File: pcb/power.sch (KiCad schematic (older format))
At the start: 8 parts

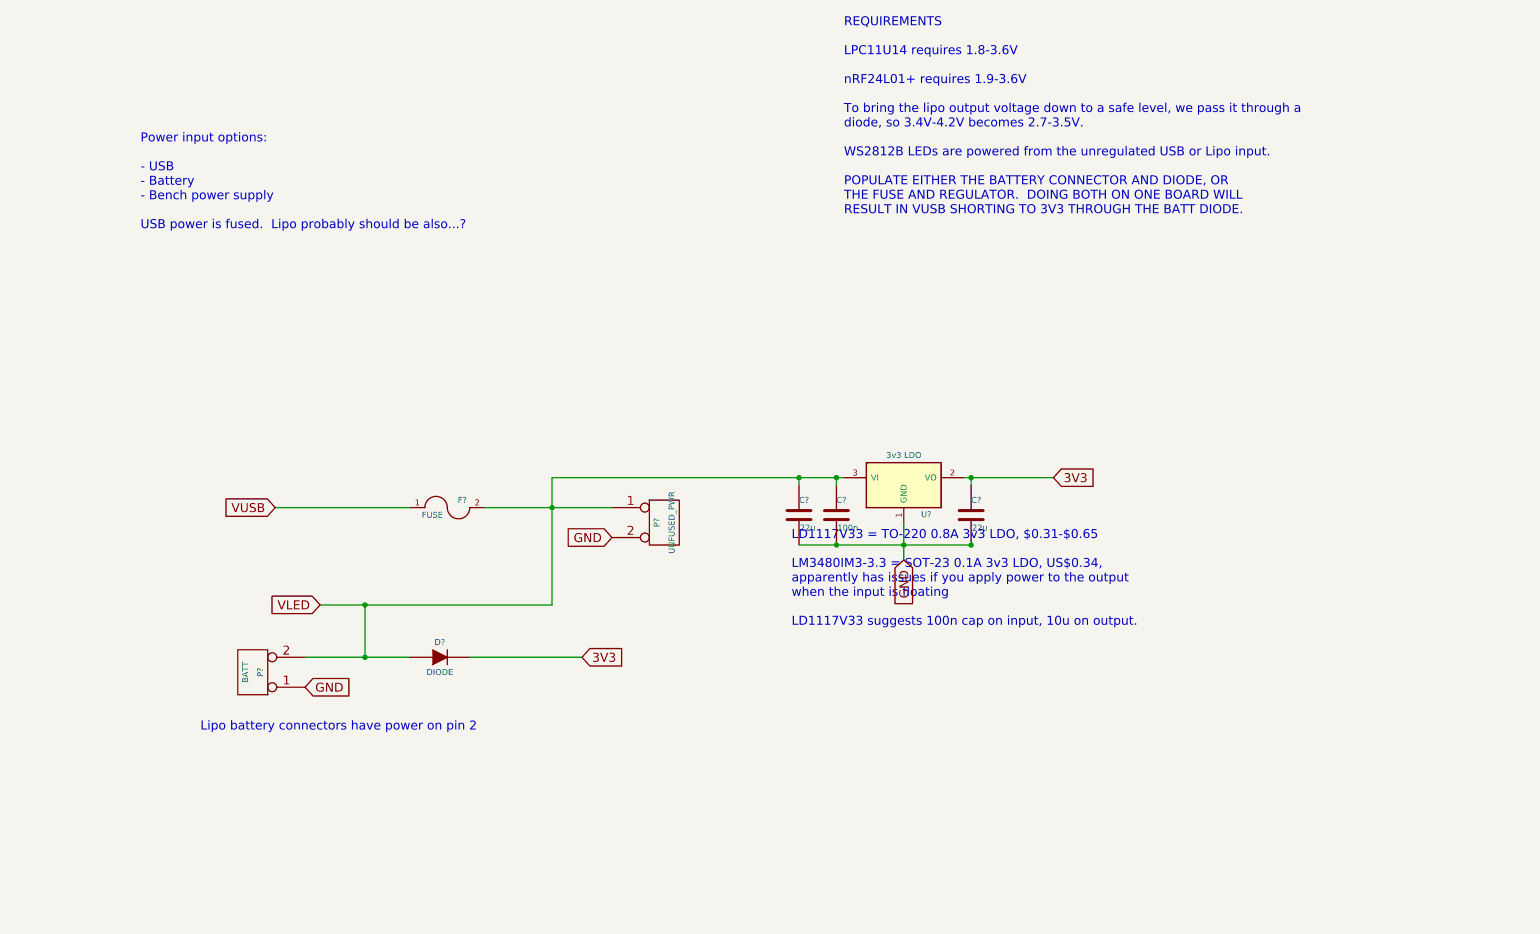
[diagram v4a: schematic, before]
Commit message: added second 3v3 ldo in parallel with the first one, so we can have the option at build time
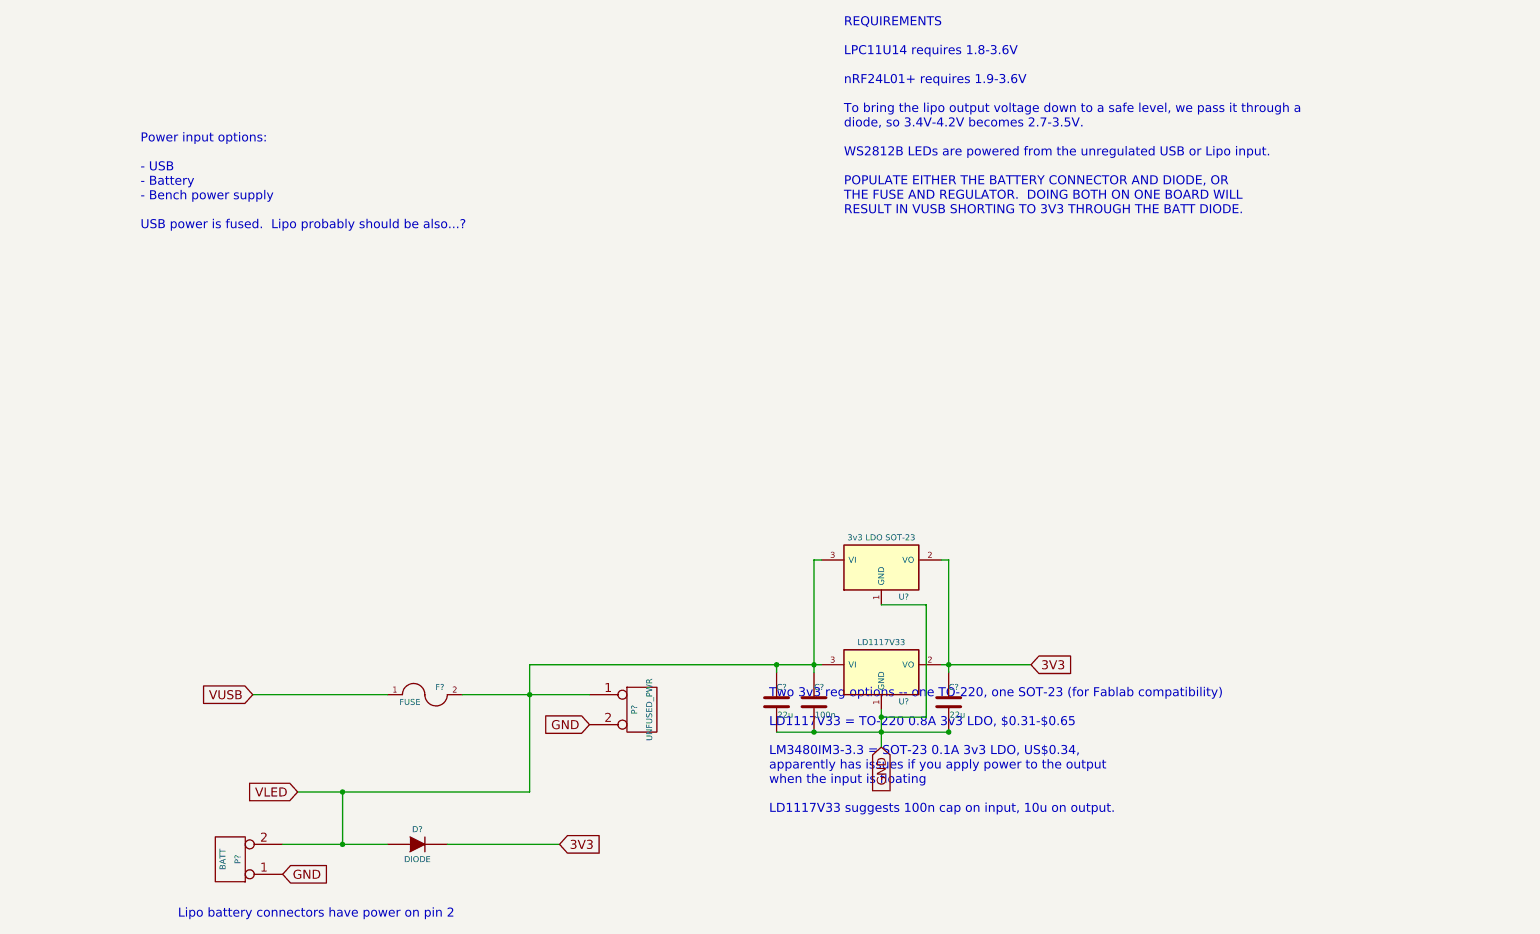
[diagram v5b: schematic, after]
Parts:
- added U?: 3v3 LDO SOT-23, ~, symbol NCP1117ST33T3G
- U?: value 3v3 LDO -> LD1117V33
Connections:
- net 3V3: now also U?.2 (VO)
- net GND: now also U?.1 (GND)
- net VLED: now also U?.3 (VI)
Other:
- note added: "Two 3v3 reg options -- one TO-220, one SOT-23 (for Fablab compatibility)\n\nLD1117V33 = TO-220 0.8A 3v3 LDO, $0.31-$0.65\n\nLM3480IM3-3.3 = SOT-23 0.1A 3v3 LDO, US$0.34,\napparently has issues if you apply power to the output\nwhen the input is floating\n\nLD1117V33 suggests 100n cap on input, 10u on output."
- note removed: "LD1117V33 = TO-220 0.8A 3v3 LDO, $0.31-$0.65\n\nLM3480IM3-3.3 = SOT-23 0.1A 3v3 LDO, US$0.34,\napparently has issues if you apply power to the output\nwhen the input is floating\n\nLD1117V33 suggests 100n cap on input, 10u on output."
- moved on the sheet: C?, D?, F?, P?, U?
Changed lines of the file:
@@
 L CONN_2 P?
 U 1 1 549D502B
-P 2750 4350
-F 0 "P?" V 2700 4350 40  0000 C CNN
-F 1 "BATT" V 2800 4350 40  0000 C CNN
-F 2 "" H 2750 4350 60  0000 C CNN
-F 3 "" H 2750 4350 60  0000 C CNN
-	1    2750 4350
+P 2600 5600
+F 0 "P?" V 2550 5600 40  0000 C CNN
+F 1 "BATT" V 2650 5600 40  0000 C CNN
+F 2 "" H 2600 5600 60  0000 C CNN
+F 3 "" H 2600 5600 60  0000 C CNN
+	1    2600 5600
 	-1   0    0    1
 $EndComp
@@
 L CONN_2 P?
 U 1 1 549D503A
-P 5500 3350
-F 0 "P?" V 5450 3350 40  0000 C CNN
-F 1 "UNFUSED_PWR" V 5550 3350 40  0000 C CNN
-F 2 "" H 5500 3350 60  0000 C CNN
-F 3 "" H 5500 3350 60  0000 C CNN
-	1    5500 3350
+P 5350 4600
+F 0 "P?" V 5300 4600 40  0000 C CNN
+F 1 "UNFUSED_PWR" V 5400 4600 40  0000 C CNN
+F 2 "" H 5350 4600 60  0000 C CNN
+F 3 "" H 5350 4600 60  0000 C CNN
+	1    5350 4600
 	1    0    0    -1
 $EndComp
-Text GLabel 2900 3250 0    60   Input ~ 0
+Text GLabel 2750 4500 0    60   Input ~ 0
 VUSB
 $Comp
 L FUSE F?
 U 1 1 549D506C
-P 4050 3250
-F 0 "F?" H 4150 3300 40  0000 C CNN
-F 1 "FUSE" H 3950 3200 40  0000 C CNN
-F 2 "~" H 4050 3250 60  0000 C CNN
-F 3 "~" H 4050 3250 60  0000 C CNN
-	1    4050 3250
+P 3900 4500
+F 0 "F?" H 4000 4550 40  0000 C CNN
+F 1 "FUSE" H 3800 4450 40  0000 C CNN
+F 2 "~" H 3900 4500 60  0000 C CNN
+F 3 "~" H 3900 4500 60  0000 C CNN
+	1    3900 4500
 	1    0    0    -1
 $EndComp
-Wire Wire Line
-	2900 3250 3800 3250
-Wire Wire Line
-	4300 3250 5150 3250
-Text GLabel 3100 4450 2    60   Input ~ 0
+Text GLabel 2950 5700 2    60   Input ~ 0
 GND
-Text GLabel 5150 3450 0    60   Input ~ 0
+Text GLabel 5000 4700 0    60   Input ~ 0
 GND
 Text Notes 2000 1400 0    60   ~ 0
 Power input options:\n\n- USB\n- Battery\n- Bench power supply\n\nUSB power is fused.  Lipo probably should be also...?
-Connection ~ 4750 3250
 $Comp
 L NCP1117ST33T3G U?
 U 1 1 549D510B
-P 7100 3100
-F 0 "U?" H 7250 2904 40  0000 C CNN
-F 1 "3v3 LDO" H 7100 3300 40  0000 C CNN
-F 2 "~" H 7100 3100 60  0000 C CNN
-F 3 "~" H 7100 3100 60  0000 C CNN
-	1    7100 3100
+P 6950 4350
+F 0 "U?" H 7100 4154 40  0000 C CNN
+F 1 "LD1117V33" H 6950 4550 40  0000 C CNN
+F 2 "~" H 6950 4350 60  0000 C CNN
+F 3 "~" H 6950 4350 60  0000 C CNN
+	1    6950 4350
 	1    0    0    -1
 $EndComp
@@
 L C C?
 U 1 1 549D5130
-P 6650 3300
-F 0 "C?" H 6650 3400 40  0000 L CNN
-F 1 "100n" H 6656 3215 40  0000 L CNN
-F 2 "~" H 6688 3150 30  0000 C CNN
-F 3 "~" H 6650 3300 60  0000 C CNN
-	1    6650 3300
+P 6500 4550
+F 0 "C?" H 6500 4650 40  0000 L CNN
+F 1 "100n" H 6506 4465 40  0000 L CNN
+F 2 "~" H 6538 4400 30  0000 C CNN
+F 3 "~" H 6500 4550 60  0000 C CNN
+	1    6500 4550
 	1    0    0    -1
 $EndComp
@@
 L C C?
 U 1 1 549D513F
-P 7550 3300
-F 0 "C?" H 7550 3400 40  0000 L CNN
-F 1 "22u" H 7556 3215 40  0000 L CNN
-F 2 "~" H 7588 3150 30  0000 C CNN
-F 3 "~" H 7550 3300 60  0000 C CNN
-	1    7550 3300
+P 7400 4550
+F 0 "C?" H 7400 4650 40  0000 L CNN
+F 1 "22u" H 7406 4465 40  0000 L CNN
+F 2 "~" H 7438 4400 30  0000 C CNN
+F 3 "~" H 7400 4550 60  0000 C CNN
+	1    7400 4550
 	1    0    0    -1
 $EndComp
-Text GLabel 7100 3600 3    60   Input ~ 0
+Text GLabel 6950 4850 3    60   Input ~ 0
 GND
-Wire Wire Line
-	7100 3350 7100 3600
-Connection ~ 7100 3500
-Wire Wire Line
-	7550 3050 7550 3100
-Wire Wire Line
-	6650 3050 6650 3100
-Text GLabel 8100 3050 2    60   Input ~ 0
+Text GLabel 7950 4300 2    60   Input ~ 0
 3V3
-Connection ~ 7550 3050
-Connection ~ 6650 3050
-Text Notes 6350 4050 0    60   ~ 0
-LD1117V33 = TO-220 0.8A 3v3 LDO, $0.31-$0.65\n\nLM3480IM3-3.3 = SOT-23 0.1A 3v3 LDO, US$0.34,\napparently has issues if you apply power to the output\nwhen the input is floating\n\nLD1117V33 suggests 100n cap on input, 10u on output.
-Text Notes 2400 4750 0    60   ~ 0
+Text Notes 6200 5300 0    60   ~ 0
+Two 3v3 reg options -- one TO-220, one SOT-23 (for Fablab compatibility)\n\nLD1117V33 = TO-220 0.8A 3v3 LDO, $0.31-$0.65\n\nLM3480IM3-3.3 = SOT-23 0.1A 3v3 LDO, US$0.34,\napparently has issues if you apply power to the output\nwhen the input is floating\n\nLD1117V33 suggests 100n cap on input, 10u on output.
+Text Notes 2250 6000 0    60   ~ 0
 Lipo battery connectors have power on pin 2
 $Comp
 L C C?
 U 1 1 549D6202
-P 6400 3300
-F 0 "C?" H 6400 3400 40  0000 L CNN
-F 1 "22u" H 6406 3215 40  0000 L CNN
-F 2 "~" H 6438 3150 30  0000 C CNN
-F 3 "~" H 6400 3300 60  0000 C CNN
-	1    6400 3300
+P 6250 4550
+F 0 "C?" H 6250 4650 40  0000 L CNN
+F 1 "22u" H 6256 4465 40  0000 L CNN
+F 2 "~" H 6288 4400 30  0000 C CNN
+F 3 "~" H 6250 4550 60  0000 C CNN
+	1    6250 4550
+	1    0    0    -1
+$EndComp
+Text Notes 6700 1300 0    60   ~ 0
+REQUIREMENTS\n\nLPC11U14 requires 1.8-3.6V\n\nnRF24L01+ requires 1.9-3.6V\n\nTo bring the lipo output voltage down to a safe level, we pass it through a\ndiode, so 3.4V-4.2V becomes 2.7-3.5V.\n\nWS2812B LEDs are powered from the unregulated USB or Lipo input.\n\nPOPULATE EITHER THE BATTERY CONNECTOR AND DIODE, OR\nTHE FUSE AND REGULATOR.  DOING BOTH ON ONE BOARD WILL\nRESULT IN VUSB SHORTING TO 3V3 THROUGH THE BATT DIODE.
+$Comp
+L DIODE D?
+U 1 1 549D6318
+P 3850 5500
+F 0 "D?" H 3850 5600 40  0000 C CNN
+F 1 "DIODE" H 3850 5400 40  0000 C CNN
+F 2 "~" H 3850 5500 60  0000 C CNN
+F 3 "~" H 3850 5500 60  0000 C CNN
+	1    3850 5500
+	1    0    0    -1
+$EndComp
+Text GLabel 4800 5500 2    60   Input ~ 0
+3V3
+Text GLabel 3050 5150 0    60   Input ~ 0
+VLED
+$Comp
+L NCP1117ST33T3G U?
+U 1 1 549DD6D6
+P 6950 3650
+F 0 "U?" H 7100 3454 40  0000 C CNN
+F 1 "3v3 LDO SOT-23" H 6950 3850 40  0000 C CNN
+F 2 "~" H 6950 3650 60  0000 C CNN
+F 3 "~" H 6950 3650 60  0000 C CNN
+	1    6950 3650
 	1    0    0    -1
 $EndComp
 Wire Wire Line
-	4750 3050 6700 3050
+	2750 4500 3650 4500
 Wire Wire Line
-	6400 3050 6400 3100
-Connection ~ 6400 3050
-Connection ~ 6650 3500
-Connection ~ 7550 3500
+	4150 4500 5000 4500
+Connection ~ 4600 4500
 Wire Wire Line
-	7550 3500 6400 3500
+	6950 4600 6950 4850
+Connection ~ 6950 4750
 Wire Wire Line
-	7500 3050 8100 3050
-Text Notes 6700 1300 0    60   ~ 0
-REQUIREMENTS\n\nLPC11U14 requires 1.8-3.6V\n\nnRF24L01+ requires 1.9-3.6V\n\nTo bring the lipo output voltage down to a safe level, we pass it through a\ndiode, so 3.4V-4.2V becomes 2.7-3.5V.\n\nWS2812B LEDs are powered from the unregulated USB or Lipo input.\n\nPOPULATE EITHER THE BATTERY CONNECTOR AND DIODE, OR\nTHE FUSE AND REGULATOR.  DOING BOTH ON ONE BOARD WILL\nRESULT IN VUSB SHORTING TO 3V3 THROUGH THE BATT DIODE.
+	7400 3600 7400 4350
 Wire Wire Line
-	4750 3900 4750 3050
-$Comp
-L DIODE D?
-U 1 1 549D6318
-P 4000 4250
-F 0 "D?" H 4000 4350 40  0000 C CNN
-F 1 "DIODE" H 4000 4150 40  0000 C CNN
-F 2 "~" H 4000 4250 60  0000 C CNN
-F 3 "~" H 4000 4250 60  0000 C CNN
-	1    4000 4250
-	1    0    0    -1
-$EndComp
+	6500 3600 6500 4350
+Connection ~ 7400 4300
+Connection ~ 6500 4300
 Wire Wire Line
-	3100 4250 3800 4250
+	4600 4300 6550 4300
 Wire Wire Line
-	4950 4250 4200 4250
-Text GLabel 4950 4250 2    60   Input ~ 0
-3V3
-Text GLabel 3200 3900 0    60   Input ~ 0
-VLED
+	6250 4300 6250 4350
+Connection ~ 6250 4300
+Connection ~ 6500 4750
+Connection ~ 7400 4750
 Wire Wire Line
-	3200 3900 4750 3900
+	7400 4750 6250 4750
 Wire Wire Line
-	3500 3900 3500 4250
-Connection ~ 3500 4250
-Connection ~ 3500 3900
+	7350 4300 7950 4300
+Wire Wire Line
+	4600 5150 4600 4300
+Wire Wire Line
+	2950 5500 3650 5500
+Wire Wire Line
+	4800 5500 4050 5500
+Wire Wire Line
+	3050 5150 4600 5150
+Wire Wire Line
+	3350 5150 3350 5500
+Connection ~ 3350 5500
+Connection ~ 3350 5150
+Wire Wire Line
+	6950 3900 7250 3900
+Wire Wire Line
+	7250 3900 7250 4650
+Wire Wire Line
+	7250 4650 6950 4650
+Connection ~ 6950 4650
+Wire Wire Line
+	6550 3600 6500 3600
+Wire Wire Line
+	7350 3600 7400 3600
 $EndSCHEMATC

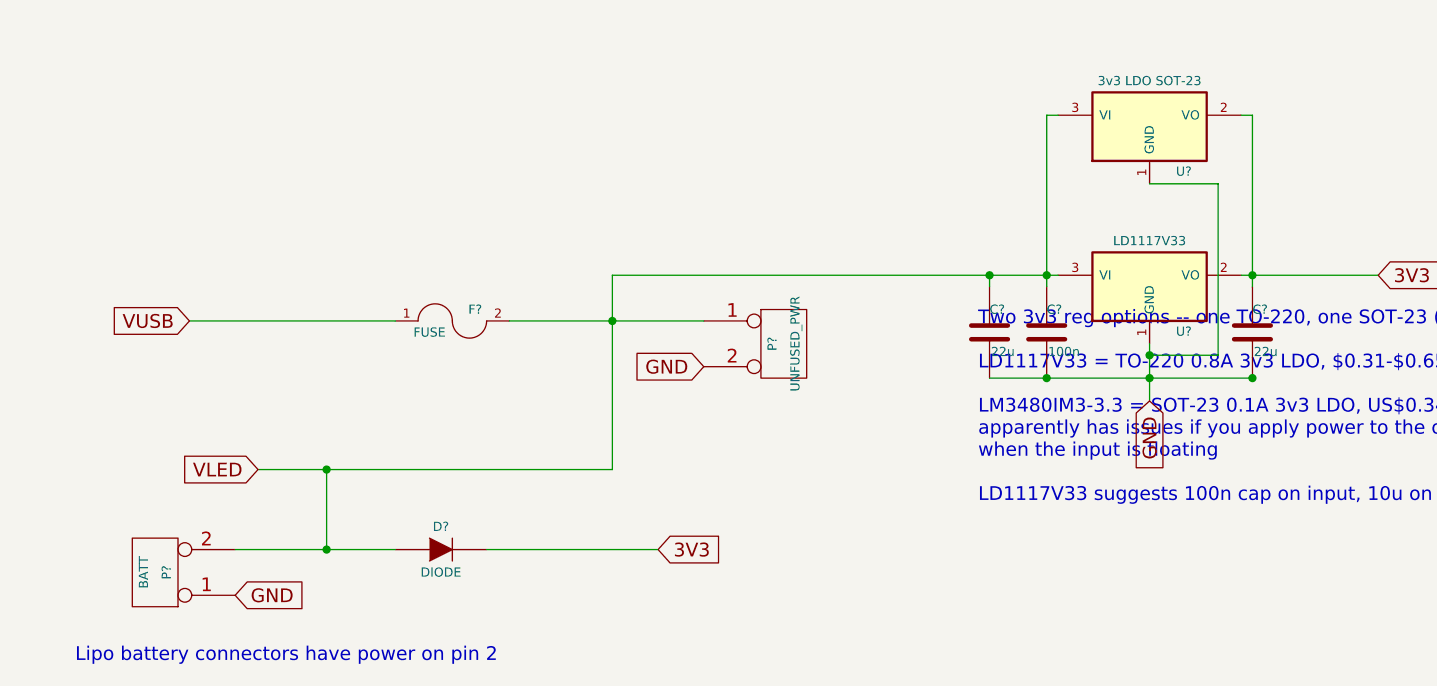
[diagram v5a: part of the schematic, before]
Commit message: made a usb-a plug from usb-if and wikipedia docs
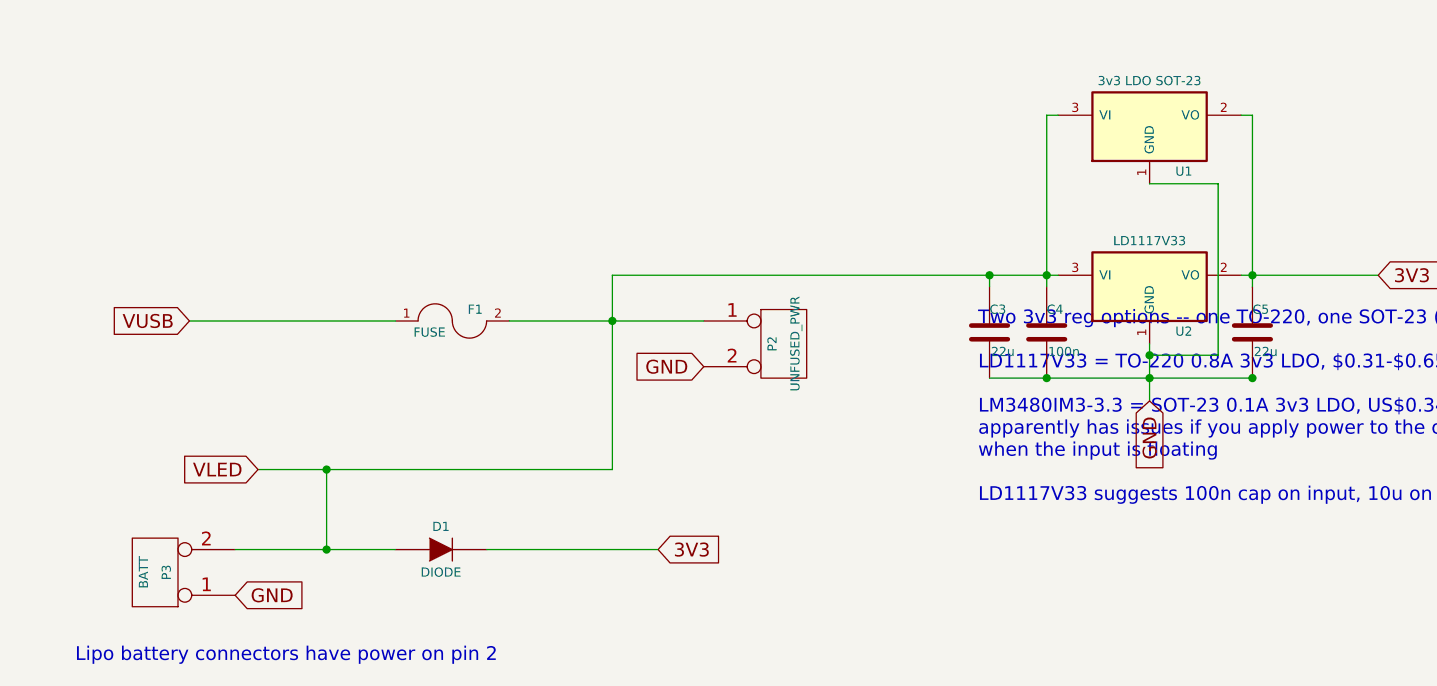
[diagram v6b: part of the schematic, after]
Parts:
- gave numbers to parts that had none: 9
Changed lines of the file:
@@
 $EndDescr
 $Comp
-L CONN_2 P?
+L CONN_2 P3
 U 1 1 549D502B
 P 2600 5600
-F 0 "P?" V 2550 5600 40  0000 C CNN
+F 0 "P3" V 2550 5600 40  0000 C CNN
 F 1 "BATT" V 2650 5600 40  0000 C CNN
 F 2 "" H 2600 5600 60  0000 C CNN
@@
 $EndComp
 $Comp
-L CONN_2 P?
+L CONN_2 P2
 U 1 1 549D503A
 P 5350 4600
-F 0 "P?" V 5300 4600 40  0000 C CNN
+F 0 "P2" V 5300 4600 40  0000 C CNN
 F 1 "UNFUSED_PWR" V 5400 4600 40  0000 C CNN
 F 2 "" H 5350 4600 60  0000 C CNN
@@
 VUSB
 $Comp
-L FUSE F?
+L FUSE F1
 U 1 1 549D506C
 P 3900 4500
-F 0 "F?" H 4000 4550 40  0000 C CNN
+F 0 "F1" H 4000 4550 40  0000 C CNN
 F 1 "FUSE" H 3800 4450 40  0000 C CNN
 F 2 "~" H 3900 4500 60  0000 C CNN
@@
 Power input options:\n\n- USB\n- Battery\n- Bench power supply\n\nUSB power is fused.  Lipo probably should be also...?
 $Comp
-L NCP1117ST33T3G U?
+L NCP1117ST33T3G U2
 U 1 1 549D510B
 P 6950 4350
-F 0 "U?" H 7100 4154 40  0000 C CNN
+F 0 "U2" H 7100 4154 40  0000 C CNN
 F 1 "LD1117V33" H 6950 4550 40  0000 C CNN
 F 2 "~" H 6950 4350 60  0000 C CNN
@@
 $EndComp
 $Comp
-L C C?
+L C C4
 U 1 1 549D5130
 P 6500 4550
-F 0 "C?" H 6500 4650 40  0000 L CNN
+F 0 "C4" H 6500 4650 40  0000 L CNN
 F 1 "100n" H 6506 4465 40  0000 L CNN
 F 2 "~" H 6538 4400 30  0000 C CNN
@@
 $EndComp
 $Comp
-L C C?
+L C C5
 U 1 1 549D513F
 P 7400 4550
-F 0 "C?" H 7400 4650 40  0000 L CNN
+F 0 "C5" H 7400 4650 40  0000 L CNN
 F 1 "22u" H 7406 4465 40  0000 L CNN
 F 2 "~" H 7438 4400 30  0000 C CNN
@@
 Lipo battery connectors have power on pin 2
 $Comp
-L C C?
+L C C3
 U 1 1 549D6202
 P 6250 4550
-F 0 "C?" H 6250 4650 40  0000 L CNN
+F 0 "C3" H 6250 4650 40  0000 L CNN
 F 1 "22u" H 6256 4465 40  0000 L CNN
 F 2 "~" H 6288 4400 30  0000 C CNN
@@
 REQUIREMENTS\n\nLPC11U14 requires 1.8-3.6V\n\nnRF24L01+ requires 1.9-3.6V\n\nTo bring the lipo output voltage down to a safe level, we pass it through a\ndiode, so 3.4V-4.2V becomes 2.7-3.5V.\n\nWS2812B LEDs are powered from the unregulated USB or Lipo input.\n\nPOPULATE EITHER THE BATTERY CONNECTOR AND DIODE, OR\nTHE FUSE AND REGULATOR.  DOING BOTH ON ONE BOARD WILL\nRESULT IN VUSB SHORTING TO 3V3 THROUGH THE BATT DIODE.
 $Comp
-L DIODE D?
+L DIODE D1
 U 1 1 549D6318
 P 3850 5500
-F 0 "D?" H 3850 5600 40  0000 C CNN
+F 0 "D1" H 3850 5600 40  0000 C CNN
 F 1 "DIODE" H 3850 5400 40  0000 C CNN
 F 2 "~" H 3850 5500 60  0000 C CNN
@@
 VLED
 $Comp
-L NCP1117ST33T3G U?
+L NCP1117ST33T3G U1
 U 1 1 549DD6D6
 P 6950 3650
-F 0 "U?" H 7100 3454 40  0000 C CNN
+F 0 "U1" H 7100 3454 40  0000 C CNN
 F 1 "3v3 LDO SOT-23" H 6950 3850 40  0000 C CNN
 F 2 "~" H 6950 3650 60  0000 C CNN

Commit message: power and usb - a bit more progress
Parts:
- added P5: BATT, symbol CONN_2
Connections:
- net GND: now also P5.2 (PM)
- net VLED: no longer names the net of C3.1, C4.1, F1.2, P2.1 (P1), U1.3 (VI), U2.3 (VI)
- net VLED: no longer D1.1 (A), P3.2 (PM)
- new net: D1.1 (A), P3.2 (PM), P5.1 (P1)
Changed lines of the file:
@@
 Text GLabel 4800 5500 2    60   Input ~ 0
 3V3
-Text GLabel 3050 5150 0    60   Input ~ 0
-VLED
 $Comp
 L NCP1117ST33T3G U1
@@
 	7350 4300 7950 4300
 Wire Wire Line
-	4600 5150 4600 4300
-Wire Wire Line
 	2950 5500 3650 5500
 Wire Wire Line
 	4800 5500 4050 5500
-Wire Wire Line
-	3050 5150 4600 5150
-Wire Wire Line
-	3350 5150 3350 5500
-Connection ~ 3350 5500
-Connection ~ 3350 5150
 Wire Wire Line
 	6950 3900 7250 3900
@@
 Wire Wire Line
 	7350 3600 7400 3600
+$Comp
+L CONN_2 P5
+U 1 1 549E81C9
+P 1850 5600
+F 0 "P5" V 1800 5600 40  0000 C CNN
+F 1 "BATT" V 1900 5600 40  0000 C CNN
+F 2 "" H 1850 5600 60  0000 C CNN
+F 3 "" H 1850 5600 60  0000 C CNN
+	1    1850 5600
+	1    0    0    -1
+$EndComp
+Wire Wire Line
+	1500 5500 1300 5500
+Wire Wire Line
+	1300 5500 1300 5300
+Wire Wire Line
+	1300 5300 3100 5300
+Wire Wire Line
+	3100 5300 3100 5500
+Connection ~ 3100 5500
+Text GLabel 1500 5700 0    60   Input ~ 0
+GND
+Wire Wire Line
+	4600 4300 4600 4500
 $EndSCHEMATC
